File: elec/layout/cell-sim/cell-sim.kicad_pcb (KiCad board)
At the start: 2 copper layers, 225.7 x 100.8 mm, 0 parts

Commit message: single cell design + layout complete
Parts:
- added C1: 16V 100nF X7R ±10% 0402 Multilayer Ceramic Capacitors MLCC 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, lib:C0402, F.Cu at (20.3, 42.8)
- added C10: 25V 1uF X5R ±10% 0402 Multilayer Ceramic Capacitors MLCC - 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, lib:C0402, F.Cu at (110.1, 45.9)
- added C11: 50V 2.2uF X5R ±10% 0805 Multilayer Ceramic Capacitors MLCC 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, lib:C0805, F.Cu at (234.4, 151.8)
- added C12: 25V 10uF X5R ±10% 0805 Multilayer Ceramic Capacitors MLCC -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, lib:C0805, F.Cu at (234.4, 156.8)
- added C13: 25V 10uF X5R ±10% 0805 Multilayer Ceramic Capacitors MLCC -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, lib:C0805, F.Cu at (234.4, 111.8)
- added C14: 25V 10uF X5R ±10% 0805 Multilayer Ceramic Capacitors MLCC -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, lib:C0805, F.Cu at (234.4, 121.8)
- added C15: 16V 100nF X7R ±10% 0402 Multilayer Ceramic Capacitors MLCC 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, lib:C0402, F.Cu at (210.1, 158.6)
- added C16: 25V 10uF X5R ±10% 0805 Multilayer Ceramic Capacitors MLCC -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, lib:C0805, F.Cu at (240.8, 111.8)
- added C17: 25V 10uF X5R ±10% 0805 Multilayer Ceramic Capacitors MLCC -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, lib:C0805, F.Cu at (253.7, 111.8)
- added C18: 25V 10uF X5R ±10% 0805 Multilayer Ceramic Capacitors MLCC -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, lib:C0805, F.Cu at (260.2, 111.8)
- added C19: 16V 100nF X7R ±10% 0402 Multilayer Ceramic Capacitors MLCC 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, lib:C0402, F.Cu at (274.0, 82.9)
- added C2: 25V 10uF X5R ±10% 0805 Multilayer Ceramic Capacitors MLCC -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, lib:C0805, F.Cu at (18.8, 42.7)
- added C20: 25V 1uF X5R ±10% 0402 Multilayer Ceramic Capacitors MLCC - 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, lib:C0402, F.Cu at (267.5, 159.0)
- added C21: 25V 10uF X5R ±10% 0805 Multilayer Ceramic Capacitors MLCC -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, lib:C0805, F.Cu at (240.8, 126.8)
- added C22: 25V 10uF X5R ±10% 0805 Multilayer Ceramic Capacitors MLCC -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, lib:C0805, F.Cu at (240.8, 121.8)
- added C23: 16V 100nF X7R ±10% 0402 Multilayer Ceramic Capacitors MLCC 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, lib:C0402, F.Cu at (275.6, 122.5)
- added C24: 16V 100nF X7R ±10% 0402 Multilayer Ceramic Capacitors MLCC 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, lib:C0402, F.Cu at (282.2, 155.0)
- added C25: 25V 1uF X5R ±10% 0402 Multilayer Ceramic Capacitors MLCC - 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, lib:C0402, F.Cu at (283.7, 79.0)
- added C26: 25V 1uF X5R ±10% 0402 Multilayer Ceramic Capacitors MLCC - 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, lib:C0402, F.Cu at (282.2, 159.0)
- added C27: 50V 2.2uF X5R ±10% 0805 Multilayer Ceramic Capacitors MLCC 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, lib:C0805, F.Cu at (247.3, 111.8)
- added C28: 25V 10uF X5R ±10% 0805 Multilayer Ceramic Capacitors MLCC -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, lib:C0805, F.Cu at (266.6, 111.8)
- added C29: 25V 10uF X5R ±10% 0805 Multilayer Ceramic Capacitors MLCC -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, lib:C0805, F.Cu at (240.8, 116.8)
- added C3: 25V 10uF X5R ±10% 0805 Multilayer Ceramic Capacitors MLCC -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, lib:C0805, F.Cu at (16.7, 42.7)
- added C30: 25V 10uF X5R ±10% 0805 Multilayer Ceramic Capacitors MLCC -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, lib:C0805, F.Cu at (260.3, 105.0)
- added C31: 16V 100nF X7R ±10% 0402 Multilayer Ceramic Capacitors MLCC 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, lib:C0402, F.Cu at (278.9, 79.0)
- added C32: 25V 10uF X5R ±10% 0805 Multilayer Ceramic Capacitors MLCC -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, lib:C0805, F.Cu at (273.2, 105.0)
- added C33: 25V 10uF X5R ±10% 0805 Multilayer Ceramic Capacitors MLCC -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, lib:C0805, F.Cu at (234.4, 141.8)
- added C34: 25V 10uF X5R ±10% 0805 Multilayer Ceramic Capacitors MLCC -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, lib:C0805, F.Cu at (279.5, 111.8)
- added C35: 16V 100nF X7R ±10% 0402 Multilayer Ceramic Capacitors MLCC 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, lib:C0402, F.Cu at (277.4, 155.0)
- added C36: 25V 1uF X5R ±10% 0402 Multilayer Ceramic Capacitors MLCC - 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, lib:C0402, F.Cu at (280.4, 122.5)
- added C37: 25V 10uF X5R ±10% 0805 Multilayer Ceramic Capacitors MLCC -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, lib:C0805, F.Cu at (247.4, 105.0)
- added C38: 25V 10uF X5R ±10% 0805 Multilayer Ceramic Capacitors MLCC -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, lib:C0805, F.Cu at (273.1, 111.8)
- added C39: 16V 100nF X7R ±10% 0402 Multilayer Ceramic Capacitors MLCC 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, lib:C0402, F.Cu at (277.4, 159.0)
- added C4: 16V 100nF X7R ±10% 0402 Multilayer Ceramic Capacitors MLCC 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, lib:C0402, F.Cu at (67.9, 45.4)
- added C40: 16V 100nF X7R ±10% 0402 Multilayer Ceramic Capacitors MLCC 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, lib:C0402, F.Cu at (270.7, 122.5)
- added C41: 25V 1uF X5R ±10% 0402 Multilayer Ceramic Capacitors MLCC - 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, lib:C0402, F.Cu at (227.1, 157.2)
- added C42: 25V 1uF X5R ±10% 0402 Multilayer Ceramic Capacitors MLCC - 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, lib:C0402, F.Cu at (262.6, 159.0)
- added C43: 50V 2.2uF X5R ±10% 0805 Multilayer Ceramic Capacitors MLCC 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, lib:C0805, F.Cu at (234.4, 131.8)
- added C44: 25V 10uF X5R ±10% 0805 Multilayer Ceramic Capacitors MLCC -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, lib:C0805, F.Cu at (234.4, 146.8)
- added C45: 25V 10uF X5R ±10% 0805 Multilayer Ceramic Capacitors MLCC -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, lib:C0805, F.Cu at (240.8, 131.8)
- added C46: 25V 10uF X5R ±10% 0805 Multilayer Ceramic Capacitors MLCC -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, lib:C0805, F.Cu at (266.7, 105.0)
- added C47: 16V 100nF X7R ±10% 0402 Multilayer Ceramic Capacitors MLCC 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, lib:C0402, F.Cu at (205.3, 158.6)
- added C48: 25V 10uF X5R ±10% 0805 Multilayer Ceramic Capacitors MLCC -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, lib:C0805, F.Cu at (234.4, 126.8)
- added C49: 25V 10uF X5R ±10% 0805 Multilayer Ceramic Capacitors MLCC -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, lib:C0805, F.Cu at (279.6, 105.0)
- added C5: 16V 2.2uF X5R ±10% 0603 Multilayer Ceramic Capacitors MLCC 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, lib:C0603, F.Cu at (69.2, 45.3)
- added C50: 25V 10uF X5R ±10% 0805 Multilayer Ceramic Capacitors MLCC -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, lib:C0805, F.Cu at (234.4, 116.8)
- added C51: 16V 100nF X7R ±10% 0402 Multilayer Ceramic Capacitors MLCC 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, lib:C0402, F.Cu at (283.9, 116.2)
- added C52: 25V 1uF X5R ±10% 0402 Multilayer Ceramic Capacitors MLCC - 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, lib:C0402, F.Cu at (282.6, 89.3)
- added C53: 25V 10uF X5R ±10% 0805 Multilayer Ceramic Capacitors MLCC -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, lib:C0805, F.Cu at (253.8, 105.0)
- added C54: 25V 10uF X5R ±10% 0805 Multilayer Ceramic Capacitors MLCC -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, lib:C0805, F.Cu at (234.4, 136.8)
- added C55: 16V 100nF X7R ±10% 0402 Multilayer Ceramic Capacitors MLCC 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, lib:C0402, F.Cu at (274.0, 79.0)
- added C56: 16V 100nF X7R ±10% 0402 Multilayer Ceramic Capacitors MLCC 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, lib:C0402, F.Cu at (282.6, 93.2)
- added C57: 25V 1uF X5R ±10% 0402 Multilayer Ceramic Capacitors MLCC - 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, lib:C0402, F.Cu at (257.7, 159.0)
- added C58: 25V 1uF X5R ±10% 0402 Multilayer Ceramic Capacitors MLCC - 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, lib:C0402, F.Cu at (272.4, 159.0)
- added C6: 6.3V 10uF X5R ±20% 0402 Multilayer Ceramic Capacitors MLCC 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, lib:C0402, F.Cu at (94.7, 41.6)
- added C7: 25V 10uF X5R ±10% 0805 Multilayer Ceramic Capacitors MLCC -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, lib:C0805, F.Cu at (91.0, 41.7)
- added C8: 16V 100nF X7R ±10% 0402 Multilayer Ceramic Capacitors MLCC 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, lib:C0402, F.Cu at (94.5, 46.3)
- added C9: 25V 1uF X5R ±10% 0402 Multilayer Ceramic Capacitors MLCC - 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, lib:C0402, F.Cu at (114.6, 45.9)
- added DS1: , lib:SOD-323_L1.8-W1.3-LS2.5-RD, F.Cu at (94.9, 47.6)
- added DS2: , lib:SOD-323_L1.8-W1.3-LS2.5-RD, F.Cu at (240.8, 151.5)
- added L1: , lib:IND-SMD_L4.0-W4.0, F.Cu at (90.6, 45.4)
- added L2: , lib:IND-SMD_L4.4-W4.2, F.Cu at (220.3, 124.4)
- added L3: 100uH, lib:IND-SMD_L4.0-W4.0, F.Cu at (220.0, 139.3)
- added L4: , lib:IND-SMD_L4.4-W4.2, F.Cu at (220.3, 131.9)
- added L5: 100uH, lib:IND-SMD_L4.0-W4.0, F.Cu at (220.0, 146.7)
- added L6: , lib:IND-SMD_L4.4-W4.2, F.Cu at (220.3, 116.9)
- added L7: 100uH, lib:IND-SMD_L4.0-W4.0, F.Cu at (220.0, 154.0)
- added LED1: , lib:LED0603-RD, F.Cu at (247.1, 138.1)
- added LED2: , lib:LED0603-RD, F.Cu at (259.3, 122.8)
- added LED3: , lib:LED0603-RD, F.Cu at (265.3, 122.8)
- added LED4: , lib:LED0603-RD, F.Cu at (247.1, 156.7)
- added LED5: , lib:LED0603-RD, F.Cu at (247.1, 152.0)
- added LED6: , lib:LED0603-RD, F.Cu at (247.1, 142.7)
- added LED7: , lib:LED0603-RD, F.Cu at (247.1, 147.4)
- added LED8: , lib:LED0603-RD, F.Cu at (247.1, 133.4)
- added LED9: , lib:LED0603-RD, F.Cu at (253.2, 122.8)
- added Q1: , lib:SOT-23-3_L2.9-W1.3-P1.90-LS2.4-BR, F.Cu at (240.7, 156.9)
- added Q2: , lib:SOT-23-3_L2.9-W1.3-P1.90-LS2.4-BR, F.Cu at (259.7, 117.4)
- added Q3: , lib:SOT-23-3_L2.9-W1.3-P1.90-LS2.4-BR, F.Cu at (253.4, 117.4)
- added Q4: , lib:SOT-23-3_L2.9-W1.3-P1.90-LS2.4-BR, F.Cu at (272.2, 117.4)
- added Q5: , lib:SOT-23-3_L2.9-W1.3-P1.90-LS2.4-BR, F.Cu at (265.9, 117.4)
- added Q6: , lib:SOT-23-3_L2.9-W1.3-P1.90-LS2.4-BR, F.Cu at (247.2, 117.4)
- added R1: 62.5mW Thick Film Resistors 50V ±100ppm/℃ ±1% 10kΩ 0402 Chi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, lib:R0402, F.Cu at (19.7, 45.5)
- added R10: 62.5mW Thick Film Resistors 50V ±100ppm/℃ ±1% 10kΩ 0402 Chi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, lib:R0402, F.Cu at (78.4, 51.3)
- added R11: 62.5mW Thick Film Resistors 50V ±100ppm/℃ ±1% 10kΩ 0402 Chi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, lib:R0402, F.Cu at (77.3, 51.3)
- added R12: 62.5mW Thick Film Resistors 50V ±100ppm/℃ ±1% 10kΩ 0402 Chi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, lib:R0402, F.Cu at (77.2, 38.9)
- added R13: 62.5mW Thick Film Resistors 50V ±100ppm/℃ ±1% 10kΩ 0402 Chi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, lib:R0402, F.Cu at (78.2, 38.9)
- added R14: 62.5mW Thick Film Resistors 50V ±100ppm/℃ ±1% 10kΩ 0402 Chi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, lib:R0402, F.Cu at (75.1, 38.9)
- added R15: 62.5mW Thick Film Resistors 50V ±100ppm/℃ ±1% 10kΩ 0402 Chi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, lib:R0402, F.Cu at (76.1, 38.9)
- added R16: 62.5mW Thick Film Resistors 50V ±100ppm/℃ ±1% 10kΩ 0402 Chi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, lib:R0402, F.Cu at (73.0, 38.9)
- added R17: 62.5mW Thick Film Resistors 50V ±100ppm/℃ ±1% 10kΩ 0402 Chi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, lib:R0402, F.Cu at (74.0, 38.9)
- added R18: 62.5mW Thick Film Resistors 50V ±100ppm/℃ ±1% 10kΩ 0402 Chi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, lib:R0402, F.Cu at (70.9, 38.9)
- added R19: 62.5mW Thick Film Resistors 50V ±100ppm/℃ ±1% 10kΩ 0402 Chi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, lib:R0402, F.Cu at (71.9, 38.9)
- added R2: 62.5mW Thick Film Resistors 50V ±100ppm/℃ ±1% 4.7kΩ 0402 Ch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, lib:R0402, F.Cu at (50.3, 47.0)
- added R20: 62.5mW Thin Film Resistor 50V ±25ppm/℃ ±0.1% 22.6kΩ 0402 Ch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, lib:R0402, F.Cu at (92.1, 40.1)
- added R21: 62.5mW Thick Film Resistors 50V ±1% ±100ppm/℃ 4.12kΩ 0402 C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, lib:R0402, F.Cu at (90.2, 40.1)
- added R22: 62.5mW Thick Film Resistors 50V ±100ppm/℃ ±1% 17.4kΩ 0402 C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, lib:R0402, F.Cu at (111.4, 43.6)
- added R23: 62.5mW Thick Film Resistors 50V ±100ppm/℃ ±1% 10.2kΩ 0402 C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, lib:R0402, F.Cu at (113.4, 43.6)
- added R24: 62.5mW Thick Film Resistors 50V ±100ppm/℃ ±1% 10kΩ 0402 Chi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, lib:R0402, F.Cu at (130.3, 45.2)
- added R25: 62.5mW Thick Film Resistors 50V ±100ppm/℃ ±1% 10kΩ 0402 Chi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, lib:R0402, F.Cu at (127.7, 47.5)
- added R26: 62.5mW Thick Film Resistors 50V ±100ppm/℃ ±1% 21kΩ 0402 Chi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, lib:R0402, F.Cu at (267.6, 155.0)
- added R27: 62.5mW Thick Film Resistors 50V ±100ppm/℃ ±1% 24kΩ 0402 Chi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, lib:R0402, F.Cu at (257.7, 155.0)
- added R28: 62.5mW Thick Film Resistors 50V ±100ppm/℃ ±1% 37.4kΩ 0402 C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, lib:R0402, F.Cu at (272.5, 151.1)
- added R29: 62.5mW Thick Film Resistors 50V ±100ppm/℃ ±1% 10kΩ 0402 Chi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, lib:R0402, F.Cu at (267.6, 131.1)
- added R3: 62.5mW Thick Film Resistors 50V ±100ppm/℃ ±1% 4.7kΩ 0402 Ch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, lib:R0402, F.Cu at (53.3, 46.9)
- added R30: 62.5mW Thick Film Resistors 50V ±100ppm/℃ ±1% 10kΩ 0402 Chi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, lib:R0402, F.Cu at (277.4, 147.1)
- added R31: 62.5mW Thick Film Resistors 50V ±100ppm/℃ ±1% 43kΩ 0402 Chi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, lib:R0402, F.Cu at (267.6, 143.1)
- added R32: 62.5mW Thick Film Resistors 50V ±100ppm/℃ ±1% 60.4kΩ 0402 C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, lib:R0402, F.Cu at (267.6, 139.1)
- added R33: 62.5mW Thick Film Resistors 50V ±100ppm/℃ ±1% 10kΩ 0402 Chi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, lib:R0402, F.Cu at (262.6, 155.0)
- added R34: 62.5mW Thick Film Resistors 50V ±100ppm/℃ ±1% 10kΩ 0402 Chi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, lib:R0402, F.Cu at (277.4, 135.1)
- added R35: 125mW Thick Film Resistors 150V ±1% 100mΩ 0805 Chip Resisto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, lib:R0805, F.Cu at (240.8, 146.7)
- added R36: 62.5mW Thick Film Resistors 50V ±100ppm/℃ ±1% 21kΩ 0402 Chi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, lib:R0402, F.Cu at (257.7, 127.1)
- added R37: 62.5mW Thick Film Resistors 50V ±100ppm/℃ ±1% 10kΩ 0402 Chi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, lib:R0402, F.Cu at (267.6, 135.1)
- added R38: 62.5mW Thick Film Resistors 50V ±100ppm/℃ ±1% 1kΩ 0402 Chip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, lib:R0402, F.Cu at (277.4, 131.1)
- added R39: 62.5mW Thick Film Resistors 50V ±100ppm/℃ ±1% 21kΩ 0402 Chi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, lib:R0402, F.Cu at (267.6, 147.1)
- added R4: 62.5mW Thick Film Resistors 50V ±100ppm/℃ ±1% 10kΩ 0402 Chi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, lib:R0402, F.Cu at (71.9, 51.3)
- added R40: 62.5mW Thick Film Resistors 50V ±100ppm/℃ ±1% 10kΩ 0402 Chi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, lib:R0402, F.Cu at (272.5, 147.1)
- added R41: 62.5mW Thick Film Resistors 50V ±100ppm/℃ ±1% 1kΩ 0402 Chip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, lib:R0402, F.Cu at (257.7, 143.1)
- added R42: 62.5mW Thin Film Resistor 50V ±25ppm/℃ ±1% 11.5kΩ 0402 Chip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, lib:R0402, F.Cu at (272.5, 131.1)
- added R43: 62.5mW Thick Film Resistors 50V ±100ppm/℃ ±1% 6.2kΩ 0402 Ch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, lib:R0402, F.Cu at (267.6, 127.1)
- added R44: 62.5mW Thick Film Resistors 50V ±100ppm/℃ ±1% 21kΩ 0402 Chi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, lib:R0402, F.Cu at (272.5, 127.1)
- added R45: 62.5mW Thick Film Resistors 50V ±100ppm/℃ ±1% 24kΩ 0402 Chi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, lib:R0402, F.Cu at (282.3, 131.1)
- added R46: 62.5mW Thick Film Resistors 50V ±100ppm/℃ ±1% 37.4kΩ 0402 C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, lib:R0402, F.Cu at (282.3, 135.1)
- added R47: 62.5mW Thick Film Resistors 50V ±100ppm/℃ ±1% 10kΩ 0402 Chi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, lib:R0402, F.Cu at (262.6, 131.1)
- added R48: 62.5mW Thick Film Resistors 50V ±100ppm/℃ ±1% 10kΩ 0402 Chi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, lib:R0402, F.Cu at (267.6, 151.1)
- added R49: 62.5mW Thick Film Resistors 50V ±100ppm/℃ ±1% 43kΩ 0402 Chi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, lib:R0402, F.Cu at (282.3, 147.1)
- added R5: 62.5mW Thick Film Resistors 50V ±100ppm/℃ ±1% 10kΩ 0402 Chi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, lib:R0402, F.Cu at (70.9, 51.3)
- added R50: 62.5mW Thick Film Resistors 50V ±100ppm/℃ ±1% 60.4kΩ 0402 C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, lib:R0402, F.Cu at (252.6, 157.7)
- added R51: 62.5mW Thick Film Resistors 50V ±100ppm/℃ ±1% 10kΩ 0402 Chi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, lib:R0402, F.Cu at (282.3, 139.1)
- added R52: 62.5mW Thick Film Resistors 50V ±100ppm/℃ ±1% 10kΩ 0402 Chi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, lib:R0402, F.Cu at (262.6, 143.1)
- added R53: 125mW Thick Film Resistors 150V ±1% 100mΩ 0805 Chip Resisto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, lib:R0805, F.Cu at (240.8, 141.7)
- added R54: 62.5mW Thick Film Resistors 50V ±100ppm/℃ ±1% 21kΩ 0402 Chi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, lib:R0402, F.Cu at (257.7, 131.1)
- added R55: 62.5mW Thick Film Resistors 50V ±100ppm/℃ ±1% 10kΩ 0402 Chi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, lib:R0402, F.Cu at (262.6, 127.1)
- added R56: 62.5mW Thick Film Resistors 50V ±100ppm/℃ ±1% 1kΩ 0402 Chip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, lib:R0402, F.Cu at (277.4, 139.1)
- added R57: 62.5mW Thick Film Resistors 50V ±100ppm/℃ ±1% 21kΩ 0402 Chi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, lib:R0402, F.Cu at (252.6, 141.8)
- added R58: 62.5mW Thick Film Resistors 50V ±100ppm/℃ ±1% 10kΩ 0402 Chi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, lib:R0402, F.Cu at (262.6, 151.1)
- added R59: 62.5mW Thick Film Resistors 50V ±100ppm/℃ ±1% 1kΩ 0402 Chip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, lib:R0402, F.Cu at (257.7, 135.1)
- added R6: 62.5mW Thick Film Resistors 50V ±100ppm/℃ ±1% 10kΩ 0402 Chi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, lib:R0402, F.Cu at (74.1, 51.3)
- added R60: 62.5mW Thin Film Resistor 50V ±25ppm/℃ ±1% 11.5kΩ 0402 Chip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, lib:R0402, F.Cu at (252.6, 145.7)
- added R61: 62.5mW Thick Film Resistors 50V ±100ppm/℃ ±1% 6.2kΩ 0402 Ch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, lib:R0402, F.Cu at (257.7, 151.1)
- added R62: 62.5mW Thick Film Resistors 50V ±100ppm/℃ ±1% 21kΩ 0402 Chi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, lib:R0402, F.Cu at (252.6, 153.7)
- added R63: 62.5mW Thick Film Resistors 50V ±100ppm/℃ ±1% 24kΩ 0402 Chi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, lib:R0402, F.Cu at (262.6, 139.1)
- added R64: 62.5mW Thick Film Resistors 50V ±100ppm/℃ ±1% 37.4kΩ 0402 C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, lib:R0402, F.Cu at (282.3, 143.1)
- added R65: 62.5mW Thick Film Resistors 50V ±100ppm/℃ ±1% 10kΩ 0402 Chi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, lib:R0402, F.Cu at (272.5, 135.1)
- added R66: 62.5mW Thick Film Resistors 50V ±100ppm/℃ ±1% 10kΩ 0402 Chi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, lib:R0402, F.Cu at (272.5, 139.1)
- added R67: 62.5mW Thick Film Resistors 50V ±100ppm/℃ ±1% 43kΩ 0402 Chi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, lib:R0402, F.Cu at (257.7, 147.1)
- added R68: 62.5mW Thick Film Resistors 50V ±100ppm/℃ ±1% 60.4kΩ 0402 C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, lib:R0402, F.Cu at (262.6, 147.1)
- added R69: 62.5mW Thick Film Resistors 50V ±100ppm/℃ ±1% 10kΩ 0402 Chi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, lib:R0402, F.Cu at (252.6, 149.7)
- added R7: 62.5mW Thick Film Resistors 50V ±100ppm/℃ ±1% 10kΩ 0402 Chi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, lib:R0402, F.Cu at (73.0, 51.3)
- added R70: 62.5mW Thick Film Resistors 50V ±100ppm/℃ ±1% 10kΩ 0402 Chi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, lib:R0402, F.Cu at (262.6, 135.1)
- added R71: 125mW Thick Film Resistors 150V ±1% 100mΩ 0805 Chip Resisto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, lib:R0805, F.Cu at (240.8, 136.8)
- added R72: 62.5mW Thick Film Resistors 50V ±100ppm/℃ ±1% 21kΩ 0402 Chi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, lib:R0402, F.Cu at (282.3, 151.1)
- added R73: 62.5mW Thick Film Resistors 50V ±100ppm/℃ ±1% 10kΩ 0402 Chi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, lib:R0402, F.Cu at (272.5, 143.1)
- added R74: 62.5mW Thick Film Resistors 50V ±100ppm/℃ ±1% 1kΩ 0402 Chip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, lib:R0402, F.Cu at (277.4, 151.1)
- added R75: 62.5mW Thick Film Resistors 50V ±100ppm/℃ ±1% 21kΩ 0402 Chi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, lib:R0402, F.Cu at (277.4, 143.1)
- added R76: 62.5mW Thick Film Resistors 50V ±100ppm/℃ ±1% 10kΩ 0402 Chi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, lib:R0402, F.Cu at (272.5, 155.0)
- added R77: 62.5mW Thick Film Resistors 50V ±100ppm/℃ ±1% 1kΩ 0402 Chip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, lib:R0402, F.Cu at (257.7, 139.1)
- added R78: 62.5mW Thin Film Resistor 50V ±25ppm/℃ ±1% 11.5kΩ 0402 Chip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, lib:R0402, F.Cu at (277.4, 127.1)
- added R79: 62.5mW Thick Film Resistors 50V ±100ppm/℃ ±1% 6.2kΩ 0402 Ch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, lib:R0402, F.Cu at (282.3, 127.1)
- added R8: 62.5mW Thick Film Resistors 50V ±100ppm/℃ ±1% 10kΩ 0402 Chi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, lib:R0402, F.Cu at (76.2, 51.3)
- added R9: 62.5mW Thick Film Resistors 50V ±100ppm/℃ ±1% 10kΩ 0402 Chi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, lib:R0402, F.Cu at (75.2, 51.3)
- added U1: , lib:WIRELM-SMD_ESP32-S3-WROOM-1, F.Cu at (30.7, 51.1)
- added U10: , lib:SOT-23-6_L2.9-W1.6-P0.95-LS2.8-BL, F.Cu at (247.8, 99.3)
- added U11: , lib:SOT-23-6_L2.9-W1.6-P0.95-LS2.8-BL, F.Cu at (234.7, 99.3)
- added U12: , lib:SOT-23-6_L2.9-W1.6-P0.95-LS2.8-BL, F.Cu at (228.1, 99.3)
- added U13: , lib:WSON-6_L2.0-W2.0-P0.65-TL-EP, F.Cu at (247.3, 128.4)
- added U14: , lib:SOT-563_L1.6-W1.2-P0.50-LS1.6-TL, F.Cu at (252.7, 132.5)
- added U15: , lib:RELAY-SMD_HFD4-5-SR, F.Cu at (209.5, 104.6)
- added U16: , lib:RELAY-SMD_HFD4-5-SR, F.Cu at (209.5, 116.1)
- added U17: , lib:QFN-16_L3.0-W3.0-P0.50-BL-EP1.7, F.Cu at (240.9, 105.7)
- added U18: , lib:SOIC-8_L4.9-W3.9-P1.27-LS6.0-TL, F.Cu at (231.1, 92.0)
- added U19: , lib:LED-SMD_4P-L2.0-W2.0-BR, F.Cu at (250.4, 91.5)
- added U2: , lib:KEY-SMD_4P-L4.2-W3.2-P2.20-LS4.6, F.Cu at (17.5, 47.5)
- added U20: , lib:LED-SMD_4P-L2.0-W2.0-BR, F.Cu at (258.9, 91.5)
- added U21: , lib:SOT-23-5_L3.0-W1.7-P0.95-LS2.8-BL, F.Cu at (228.1, 118.6)
- added U22: , lib:PWRM-TH_BXXXXS-2WR2, F.Cu at (235.9, 79.5)
- added U23: , lib:MSOP-10_L3.0-W3.0-P0.50-LS5.0-BL, F.Cu at (228.0, 144.0)
- added U24: , lib:SOT-23-6_L2.9-W1.6-P0.95-LS2.8-BL, F.Cu at (267.6, 99.3)
- added U25: , lib:SOT-23-6_L2.9-W1.6-P0.95-LS2.8-BL, F.Cu at (261.0, 99.3)
- added U26: , lib:SOT-23-6_L2.9-W1.6-P0.95-LS2.8-BL, F.Cu at (274.1, 99.3)
- added U27: , lib:WSON-6_L2.0-W2.0-P0.65-TL-EP, F.Cu at (278.6, 116.9)
- added U28: , lib:SOT-563_L1.6-W1.2-P0.50-LS1.6-TL, F.Cu at (252.7, 127.7)
- added U29: , lib:RELAY-SMD_HFD4-5-SR, F.Cu at (209.5, 139.3)
- added U3: , lib:USB-C-SMD_KH-TYPE-C-16P, F.Cu at (51.6, 51.5)
- added U30: , lib:RELAY-SMD_HFD4-5-SR, F.Cu at (209.5, 127.7)
- added U31: , lib:QFN-16_L3.0-W3.0-P0.50-BL-EP1.7, F.Cu at (227.9, 151.6)
- added U32: , lib:SOIC-8_L4.9-W3.9-P1.27-LS6.0-TL, F.Cu at (221.1, 92.0)
- added U33: , lib:LED-SMD_4P-L2.0-W2.0-BR, F.Cu at (267.4, 91.5)
- added U34: , lib:LED-SMD_4P-L2.0-W2.0-BR, F.Cu at (275.9, 91.5)
- added U35: , lib:SOT-23-5_L3.0-W1.7-P0.95-LS2.8-BL, F.Cu at (228.1, 112.2)
- added U36: , lib:PWRM-TH_BXXXXS-2WR2, F.Cu at (258.8, 79.5)
- added U37: , lib:MSOP-10_L3.0-W3.0-P0.50-LS5.0-BL, F.Cu at (228.0, 126.3)
- added U38: , lib:SOT-23-6_L2.9-W1.6-P0.95-LS2.8-BL, F.Cu at (241.2, 99.3)
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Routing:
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- added copper zone on F.Cu, net buck.ic-sw
- added copper zone on F.Cu, net vcc
- added copper zone on F.Cu, net vcc-2
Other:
- board outline removed
- copper layers 2 -> 4

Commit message: layout progress
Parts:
- moved C24 232.8 mm to (55.3, 103.2), turned to -90 degrees
- moved C39 230.6 mm to (55.3, 96.9), turned to -90 degrees
- moved C56 227.4 mm to (55.3, 85.1), turned to -90 degrees
- moved C23 220.9 mm to (55.3, 106.0), turned to -90 degrees
- moved C55 218.9 mm to (55.3, 87.9), turned to -90 degrees
- moved U34 218.8 mm to (57.1, 93.9), turned to 180 degrees
- moved C40 217.3 mm to (55.3, 94.1), turned to -90 degrees
- moved U33 210.4 mm to (57.1, 96.7), turned to 180 degrees
- moved U20 202.2 mm to (57.0, 103.0), turned to 180 degrees
- moved C26 200.4 mm to (88.6, 107.0), turned to -90 degrees
- moved C25 199.1 mm to (86.6, 107.0), turned to -90 degrees
- moved C58 196.7 mm to (88.6, 88.9), turned to -90 degrees
- moved R79 196.4 mm to (89.7, 88.9), turned to -90 degrees
- moved R64 194.0 mm to (97.0, 85.3), turned to 90 degrees
- moved U19 193.9 mm to (57.0, 105.8), turned to 180 degrees
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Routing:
- net cell2-gnd-1: track 0.00 -> 91.9 mm, vias 0 -> 26
- net cell1-gnd: track 0.00 -> 91.9 mm, vias 0 -> 26
- net cell3-gnd-1: track 0.00 -> 91.9 mm, vias 0 -> 26
- net cell2-vcc-1: track 0.00 -> 87.6 mm, vias 0 -> 3
- net cell3-vcc-1: track 0.00 -> 87.6 mm, vias 0 -> 3
- net cell1-vcc-1: track 0.00 -> 87.6 mm, vias 0 -> 3
- net gnd: track 23.1 -> 67.0 mm, vias 4 -> 19
- net cell3-scl: track 0.00 -> 43.3 mm, vias 0 -> 5
- net cell1-scl: track 0.00 -> 43.3 mm, vias 0 -> 5
- net cell2-scl: track 0.00 -> 43.3 mm, vias 0 -> 5
- net cell3-sda: track 0.00 -> 40.6 mm, vias 0 -> 4
- net cell2-sda: track 0.00 -> 40.6 mm, vias 0 -> 4
- net cell1-sda: track 0.00 -> 40.6 mm, vias 0 -> 4
- net io41: track 0.00 -> 38.4 mm, vias 0 -> 6
- net cell2.dmm_relay-input: track 0.00 -> 38.0 mm, vias 0 -> 2
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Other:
- board text added: "CellN"
- board text added: "I"
- board text added: "V"

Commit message: layout complete
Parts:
- added J1: , lib:CONN-TH_XT30PW-M, F.Cu at (64.1, 127.1)
- added R20: 62.5mW Thick Film Resistors 50V ±100ppm/℃ ±1% 2.2kΩ 0402 Ch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, lib:R0402, F.Cu at (75.2, 124.5)
- added R21: 62.5mW Thick Film Resistors 50V ±100ppm/℃ ±1% 2.2kΩ 0402 Ch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, lib:R0402, F.Cu at (75.7, 121.4)
- added R82: 62.5mW Thick Film Resistors 50V ±100ppm/℃ ±1% 1kΩ 0402 Chip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, lib:R0402, F.Cu at (70.1, 75.9)
- added R83: 62.5mW Thick Film Resistors 50V ±100ppm/℃ ±1% 1kΩ 0402 Chip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, lib:R0402, F.Cu at (72.6, 75.9)
- added R84: 62.5mW Thick Film Resistors 50V ±100ppm/℃ ±1% 1kΩ 0402 Chip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, lib:R0402, F.Cu at (75.2, 75.9)
- added R85: 62.5mW Thick Film Resistors 50V ±100ppm/℃ ±1% 1kΩ 0402 Chip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, lib:R0402, F.Cu at (77.7, 75.9)
- added R86: 62.5mW Thick Film Resistors 50V ±100ppm/℃ ±1% 1kΩ 0402 Chip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, lib:R0402, F.Cu at (92.8, 76.2)
- added R87: 62.5mW Thick Film Resistors 50V ±100ppm/℃ ±1% 1kΩ 0402 Chip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, lib:R0402, F.Cu at (95.3, 76.2)
- added R88: 62.5mW Thick Film Resistors 50V ±100ppm/℃ ±1% 1kΩ 0402 Chip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, lib:R0402, F.Cu at (97.9, 76.2)
- added R89: 62.5mW Thick Film Resistors 50V ±100ppm/℃ ±1% 1kΩ 0402 Chip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, lib:R0402, F.Cu at (100.4, 76.2)
- added R90: 62.5mW Thick Film Resistors 50V ±100ppm/℃ ±1% 1kΩ 0402 Chip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, lib:R0402, F.Cu at (115.5, 76.2)
- added R91: 62.5mW Thick Film Resistors 50V ±100ppm/℃ ±1% 1kΩ 0402 Chip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, lib:R0402, F.Cu at (118.1, 76.2)
- added R92: 62.5mW Thick Film Resistors 50V ±100ppm/℃ ±1% 1kΩ 0402 Chip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, lib:R0402, F.Cu at (120.6, 76.2)
- added R93: 62.5mW Thick Film Resistors 50V ±100ppm/℃ ±1% 1kΩ 0402 Chip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, lib:R0402, F.Cu at (123.2, 76.2)
- added U4: , lib:AUDIO-TH_24.243.1, F.Cu at (130.3, 122.4)
- added U5: , lib:CONN-TH_24.243.2, F.Cu at (141.2, 122.6)
- added U52: , lib:HDR-SMD_8P-P2.54-V-M-R2-C4-LS7.4, F.Cu at (73.9, 70.4)
- added U53: , lib:HDR-SMD_8P-P2.54-V-M-R2-C4-LS7.4, F.Cu at (96.6, 70.6)
- added U54: , lib:HDR-SMD_8P-P2.54-V-M-R2-C4-LS7.4, F.Cu at (119.4, 70.6)
- R22: renamed from R20; value 62.5mW Thin Film Resistor 50V ±25ppm/℃ ±0.1% 22.6kΩ 0402 Chip Resistor - Surface Mount ROHS -> 62.5mW Thick Film Resistors 50V ±1% ±200ppm/℃ 22.6kΩ 0402 Chip Resistor - Surface Mount ROHS
- R34: renamed from R32; value 62.5mW Thick Film Resistors 50V ±100ppm/℃ ±1% 60.4kΩ 0402 Chip Resistor - Surface Mount ROHS -> 62.5mW Thick Film Resistors 50V ±100ppm/℃ ±1% 59kΩ 0402 Chip Resistor - Surface Mount ROHS
- R37: renamed from R35; value 125mW Thick Film Resistors 150V ±1% 100mΩ 0805 Chip Resistor - Surface Mount ROHS -> 125mW Thick Film Resistors ±600ppm/℃ ±1% 110mΩ 0805 Chip Resistor - Surface Mount ROHS
- R44: renamed from R42; value 62.5mW Thin Film Resistor 50V ±25ppm/℃ ±1% 11.5kΩ 0402 Chip Resistor - Surface Mount ROHS -> 62.5mW Thick Film Resistors 50V ±100ppm/℃ ±1% 11.5kΩ 0402 Chip Resistor - Surface Mount ROHS
- R52: renamed from R50; value 62.5mW Thick Film Resistors 50V ±100ppm/℃ ±1% 60.4kΩ 0402 Chip Resistor - Surface Mount ROHS -> 62.5mW Thick Film Resistors 50V ±100ppm/℃ ±1% 59kΩ 0402 Chip Resistor - Surface Mount ROHS
- R55: renamed from R53; value 125mW Thick Film Resistors 150V ±1% 100mΩ 0805 Chip Resistor - Surface Mount ROHS -> 125mW Thick Film Resistors ±600ppm/℃ ±1% 110mΩ 0805 Chip Resistor - Surface Mount ROHS
- R62: renamed from R60; value 62.5mW Thin Film Resistor 50V ±25ppm/℃ ±1% 11.5kΩ 0402 Chip Resistor - Surface Mount ROHS -> 62.5mW Thick Film Resistors 50V ±100ppm/℃ ±1% 11.5kΩ 0402 Chip Resistor - Surface Mount ROHS
- R70: renamed from R68; value 62.5mW Thick Film Resistors 50V ±100ppm/℃ ±1% 60.4kΩ 0402 Chip Resistor - Surface Mount ROHS -> 62.5mW Thick Film Resistors 50V ±100ppm/℃ ±1% 59kΩ 0402 Chip Resistor - Surface Mount ROHS
- R73: renamed from R71; value 125mW Thick Film Resistors 150V ±1% 100mΩ 0805 Chip Resistor - Surface Mount ROHS -> 125mW Thick Film Resistors ±600ppm/℃ ±1% 110mΩ 0805 Chip Resistor - Surface Mount ROHS
- R80: renamed from R78; value 62.5mW Thin Film Resistor 50V ±25ppm/℃ ±1% 11.5kΩ 0402 Chip Resistor - Surface Mount ROHS -> 62.5mW Thick Film Resistors 50V ±100ppm/℃ ±1% 11.5kΩ 0402 Chip Resistor - Surface Mount ROHS
- moved C5 5.38 mm to (68.8, 118.7)
- moved R10 5.38 mm to (74.7, 109.5)
- moved R11 5.38 mm to (74.7, 110.6)
- moved R16 5.38 mm to (62.3, 114.9)
- moved R19 5.38 mm to (62.3, 115.9)
- moved R4 5.38 mm to (74.7, 115.9)
- moved C4 5.38 mm to (68.8, 120.0)
- moved R12 5.38 mm to (62.3, 110.7)
- moved R13 5.38 mm to (62.3, 109.7)
- moved R14 5.38 mm to (62.3, 112.8)
- moved R15 5.38 mm to (62.3, 111.8)
- moved R17 5.38 mm to (62.3, 113.8)
- moved R18 5.38 mm to (62.3, 117.0)
- moved R5 5.38 mm to (74.7, 117.0)
- moved R6 5.38 mm to (74.7, 113.8)
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- renumbered R21 to R23, R22 to R24, R23 to R25, R24 to R26, R25 to R27, R26 to R28, R27 to R29, R28 to R30, R29 to R31, R30 to R32, R31 to R33, R33 to R35, R34 to R36, R36 to R38, R37 to R39, R38 to R40, R39 to R41, R40 to R42, R41 to R43, R43 to R45, R44 to R46, R45 to R47, R46 to R48, R47 to R49, R48 to R50, R49 to R51, R51 to R53, R52 to R54, R54 to R56, R55 to R57, R56 to R58, R57 to R59, R58 to R60, R59 to R61, R61 to R63, R62 to R64, R63 to R65, R64 to R66, R65 to R67, R66 to R68, R67 to R69, R69 to R71, R70 to R72, R72 to R74, R73 to R75, R74 to R76, R75 to R77, R76 to R78, R77 to R79, R79 to R81, U8 to U10, U9 to U11, U10 to U12, U11 to U13, U12 to U14, U13 to U15, U14 to U16, U15 to U17, U16 to U18, U17 to U19, U18 to U20, U19 to U21, U20 to U22, U21 to U23, U22 to U24, U23 to U25, U24 to U26, U25 to U27, U26 to U28, U27 to U29, U28 to U30, U29 to U31, U30 to U32, U31 to U33, U32 to U34, U33 to U35, U34 to U36, U35 to U37, U36 to U38, U37 to U39, U38 to U40, U39 to U41, U40 to U42, U41 to U43, U42 to U44, U43 to U45, U44 to U46, U45 to U47, U46 to U48, U47 to U49, U48 to U50, U49 to U51, U4 to U6, U5 to U7, U6 to U8, U7 to U9
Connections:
- C12 pad 2: cell1-gnd -> gnd
- C13 pad 2: cell1-gnd -> gnd
- C14 pad 2: cell1-gnd -> gnd
- C15 pad 2: cell1-gnd -> gnd
- C16 pad 2: cell1-gnd -> gnd
- C17 pad 2: cell1-gnd -> gnd
- C18 pad 2: cell1-gnd -> gnd
- C20 pad 2: cell1-gnd -> gnd
- C21 pad 2: cell1-gnd -> gnd
- C22 pad 1: cell1-cell -> cell1-gnd
- C22 pad 2: cell1-gnd -> gnd
- C25 pad 2: cell1-gnd -> gnd
- C26 pad 2: cell1-gnd -> gnd
- C28 pad 2: cell2-gnd-1 -> cell1-gnd
- C29 pad 2: cell2-gnd-1 -> cell1-gnd
- C30 pad 2: cell2-gnd-1 -> cell1-gnd
- C31 pad 2: cell2-gnd-1 -> cell1-gnd
- C32 pad 2: cell2-gnd-1 -> cell1-gnd
- C33 pad 2: cell2-gnd-1 -> cell1-gnd
- C34 pad 2: cell2-gnd-1 -> cell1-gnd
- C36 pad 2: cell2-gnd-1 -> cell1-gnd
- C37 pad 2: cell2-gnd-1 -> cell1-gnd
- C38 pad 1: cell2-cell -> cell2-gnd-1
- C38 pad 2: cell2-gnd-1 -> cell1-gnd
- C41 pad 2: cell2-gnd-1 -> cell1-gnd
- C42 pad 2: cell2-gnd-1 -> cell1-gnd
- C44 pad 2: cell3-gnd-1 -> cell2-gnd-1
- C45 pad 2: cell3-gnd-1 -> cell2-gnd-1
- C46 pad 2: cell3-gnd-1 -> cell2-gnd-1
- C47 pad 2: cell3-gnd-1 -> cell2-gnd-1
- C48 pad 2: cell3-gnd-1 -> cell2-gnd-1
- C49 pad 2: cell3-gnd-1 -> cell2-gnd-1
- C50 pad 2: cell3-gnd-1 -> cell2-gnd-1
- C52 pad 2: cell3-gnd-1 -> cell2-gnd-1
- C53 pad 2: cell3-gnd-1 -> cell2-gnd-1
- C54 pad 2: cell3-gnd-1 -> cell2-gnd-1
- C57 pad 2: cell3-gnd-1 -> cell2-gnd-1
- C58 pad 2: cell3-gnd-1 -> cell2-gnd-1
- L3 pad 2: cell1-cell -> cell1-gnd
- L5 pad 2: cell2-cell -> cell2-gnd-1
- Q1 pad 2: cell1-gnd -> gnd
- Q2 pad 2: cell1-gnd -> gnd
- Q3 pad 2: cell2-gnd-1 -> cell1-gnd
- Q4 pad 2: cell2-gnd-1 -> cell1-gnd
- Q5 pad 2: cell3-gnd-1 -> cell2-gnd-1
- Q6 pad 2: cell3-gnd-1 -> cell2-gnd-1
- R28 pad 2: cell1-gnd -> gnd
- R31 pad 2: cell1-gnd -> gnd
- R35 pad 2: cell1-gnd -> gnd
- R37 pad 1: cell1-cell -> cell1-gnd
- R40 pad 2: cell1-gnd -> gnd
- R43 pad 2: cell1-gnd -> gnd
- R45 pad 2: cell1-gnd -> gnd
- R46 pad 2: cell2-gnd-1 -> cell1-gnd
- R49 pad 2: cell2-gnd-1 -> cell1-gnd
- R53 pad 2: cell2-gnd-1 -> cell1-gnd
- R55 pad 1: cell2-cell -> cell2-gnd-1
- R58 pad 2: cell2-gnd-1 -> cell1-gnd
- R61 pad 2: cell2-gnd-1 -> cell1-gnd
- R63 pad 2: cell2-gnd-1 -> cell1-gnd
- R64 pad 2: cell3-gnd-1 -> cell2-gnd-1
- R67 pad 2: cell3-gnd-1 -> cell2-gnd-1
- R71 pad 2: cell3-gnd-1 -> cell2-gnd-1
- R76 pad 2: cell3-gnd-1 -> cell2-gnd-1
- R79 pad 2: cell3-gnd-1 -> cell2-gnd-1
- R81 pad 2: cell3-gnd-1 -> cell2-gnd-1
- U10 pad 4: cell1-gnd -> gnd
- U11 pad 1: cell1-gnd -> gnd
- U11 pad 3: cell1-gnd -> gnd
- U12 pad 2: cell1-gnd -> gnd
- U12 pad 6: cell1-gnd -> gnd
- U13 pad 1: cell1-gnd -> gnd
- U14 pad 2: cell1-gnd -> gnd
- U14 pad 6: cell1-gnd -> gnd
- U15 pad 3: cell1-gnd -> gnd
- U15 pad 7: cell1-gnd -> gnd
- U16 pad 2: cell1-gnd -> gnd
- U16 pad 3: cell1-cell -> cell1-gnd
- U16 pad 5: cell1-gnd -> gnd
- U17 pad 4: cell1-gnd -> gnd
- U18 pad 4: cell1-gnd -> gnd
- U19 pad 16: cell1-gnd -> gnd
- U19 pad 17: cell1-gnd -> gnd
- U19 pad 2: cell1.buck-enable -> cell1.gpio-p0
- U19 pad 3: cell1.ldo-enable -> cell1.gpio-p1
- U19 pad 4: cell1.gpio-p2 -> cell1.buck-enable
- U19 pad 5: cell1.gpio-p3 -> cell1.ldo-enable
- U19 pad 6: cell1-gnd -> gnd
- U20 pad 5: cell1-gnd -> gnd
- U23 pad 2: cell1-gnd -> gnd
- U24 pad 4: cell2-gnd-1 -> cell1-gnd
- U25 pad 1: cell2-gnd-1 -> cell1-gnd
- U25 pad 3: cell2-gnd-1 -> cell1-gnd
- U26 pad 2: cell2-gnd-1 -> cell1-gnd
- U26 pad 6: cell2-gnd-1 -> cell1-gnd
- U27 pad 1: cell2-gnd-1 -> cell1-gnd
- U28 pad 2: cell2-gnd-1 -> cell1-gnd
- U28 pad 6: cell2-gnd-1 -> cell1-gnd
- U29 pad 3: cell2-gnd-1 -> cell1-gnd
- U29 pad 7: cell2-gnd-1 -> cell1-gnd
- U30 pad 2: cell2-gnd-1 -> cell1-gnd
- U30 pad 3: cell2-cell -> cell2-gnd-1
- U30 pad 5: cell2-gnd-1 -> cell1-gnd
- U31 pad 4: cell2-gnd-1 -> cell1-gnd
- U32 pad 4: cell2-gnd-1 -> cell1-gnd
- U33 pad 16: cell2-gnd-1 -> cell1-gnd
- U33 pad 17: cell2-gnd-1 -> cell1-gnd
- U33 pad 2: cell2.buck-enable -> cell2.gpio-p0
- U33 pad 3: cell2.ldo-enable -> cell2.gpio-p1
- U33 pad 4: cell2.gpio-p2 -> cell2.buck-enable
- U33 pad 5: cell2.gpio-p3 -> cell2.ldo-enable
- U33 pad 6: cell2-gnd-1 -> cell1-gnd
- U34 pad 5: cell2-gnd-1 -> cell1-gnd
- U37 pad 2: cell2-gnd-1 -> cell1-gnd
- U38 pad 4: cell3-gnd-1 -> cell2-gnd-1
- U39 pad 1: cell3-gnd-1 -> cell2-gnd-1
- U39 pad 3: cell3-gnd-1 -> cell2-gnd-1
- U40 pad 2: cell3-gnd-1 -> cell2-gnd-1
- U40 pad 6: cell3-gnd-1 -> cell2-gnd-1
- U41 pad 1: cell3-gnd-1 -> cell2-gnd-1
- U42 pad 2: cell3-gnd-1 -> cell2-gnd-1
- U42 pad 6: cell3-gnd-1 -> cell2-gnd-1
- U43 pad 3: cell3-gnd-1 -> cell2-gnd-1
- U43 pad 7: cell3-gnd-1 -> cell2-gnd-1
- U44 pad 2: cell3-gnd-1 -> cell2-gnd-1
- U44 pad 5: cell3-gnd-1 -> cell2-gnd-1
- U45 pad 4: cell3-gnd-1 -> cell2-gnd-1
- U46 pad 4: cell3-gnd-1 -> cell2-gnd-1
- U47 pad 16: cell3-gnd-1 -> cell2-gnd-1
- U47 pad 17: cell3-gnd-1 -> cell2-gnd-1
- U47 pad 2: cell3.buck-enable -> cell3.gpio-p0
- U47 pad 3: cell3.ldo-enable -> cell3.gpio-p1
- U47 pad 4: cell3.gpio-p2 -> cell3.buck-enable
- U47 pad 5: cell3.gpio-p3 -> cell3.ldo-enable
- U47 pad 6: cell3-gnd-1 -> cell2-gnd-1
- U48 pad 5: cell3-gnd-1 -> cell2-gnd-1
- U51 pad 2: cell3-gnd-1 -> cell2-gnd-1
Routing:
- net gnd: track 67.0 -> 261.7 mm, vias 19 -> 54
- net micro.ic-sda: track 0.00 -> 104.2 mm, vias 0 -> 4
- net vcc-2: track 23.5 -> 125.3 mm, vias 6 -> 11
- net micro.ic-scl: track 0.00 -> 99.8 mm, vias 0 -> 4
- net cell3-gnd-1: track 91.9 -> 0.00 mm, vias 26 -> 0
- net vcc-3: track 16.3 -> 93.7 mm, vias 0 -> 15
- net cell2-gnd-1: track 91.9 -> 162.8 mm, vias 26 -> 32
- net vcc: track 13.0 -> 81.4 mm, vias 0 -> 1
- net gnd-2: track 0.00 -> 52.0 mm
- net vcc-4: track 0.00 -> 44.9 mm
- net dm: track 0.00 -> 40.5 mm, vias 0 -> 2
- net mux.ic-sda-3: track 2.94 -> 43.2 mm, vias 0 -> 3
- net dp: track 0.00 -> 39.1 mm, vias 0 -> 2
- net io41: track 38.4 -> 0.00 mm, vias 6 -> 0
- net hv_signal: track 5.81 -> 43.4 mm, vias 0 -> 2
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- added copper zone on B.Cu, net cell1-gnd
- added copper zone on In2.Cu, net cell1-gnd
- added copper zone on In1.Cu, net cell1-vcc-2
- added copper zone on B.Cu, net cell2-gnd-1
- added copper zone on In2.Cu, net cell2-gnd-1
- added copper zone on In1.Cu, net cell2-vcc-2
- added copper zone on In1.Cu, net cell3-vcc-2
- added copper zone on B.Cu, net gnd
- added copper zone on F.Cu, net gnd
- added copper zone on In2.Cu, net gnd
- added copper zone on B.Cu, net vcc-3
- added copper zone on In1.Cu, net vcc-3
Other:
- board outline added: 100 x 70 mm
- board text added: "12V Input"
- board text added: "Cell1"
- board text added: "Cell2"
- board text added: "Cell3"
- board text added: "Cell3 Voltage Domain!!!"
- board text added: "CellSim"
- board text added: "DMM"
- board text added: "I Out DMM 5V"
- board text added: "SCL SDA BUCK LDO"
- board text removed: "CellN"

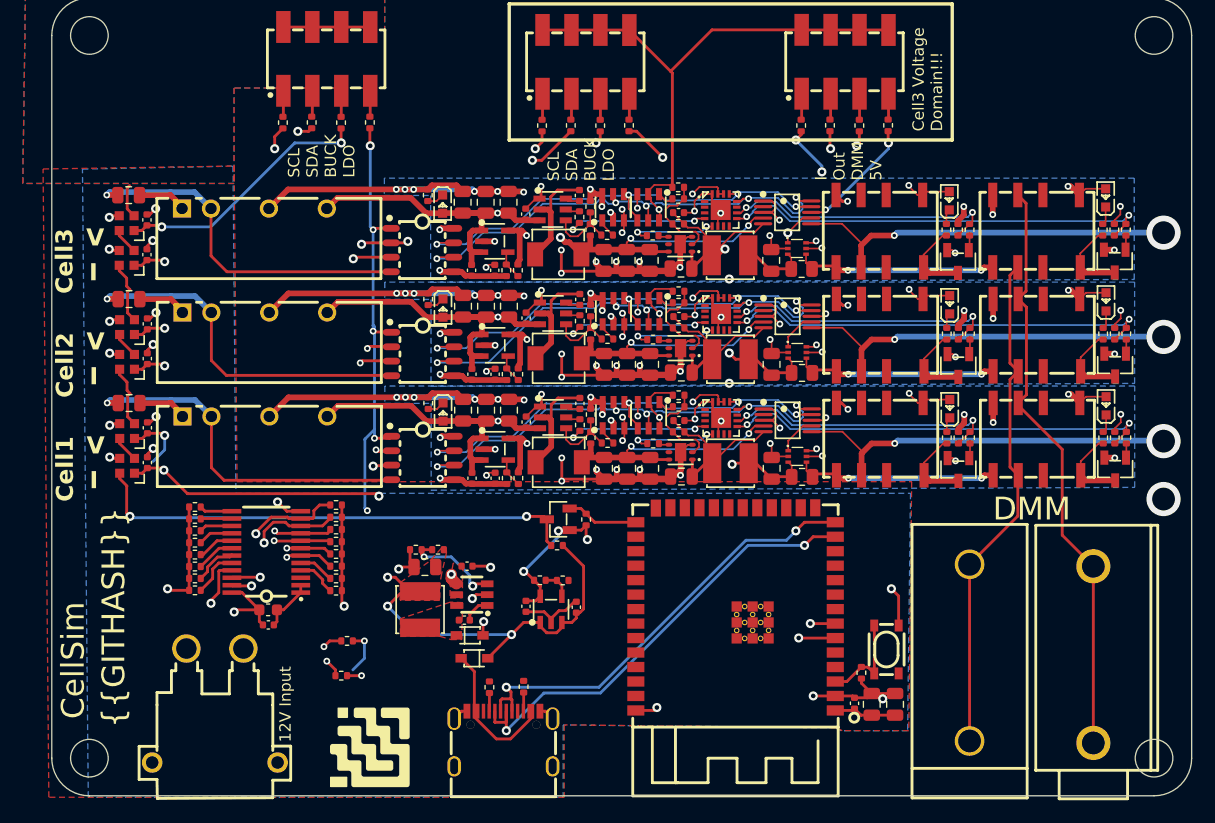
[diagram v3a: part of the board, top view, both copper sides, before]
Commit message: add reset pullup to i2c mux, add current limiting resistors to DMM connections, update layout
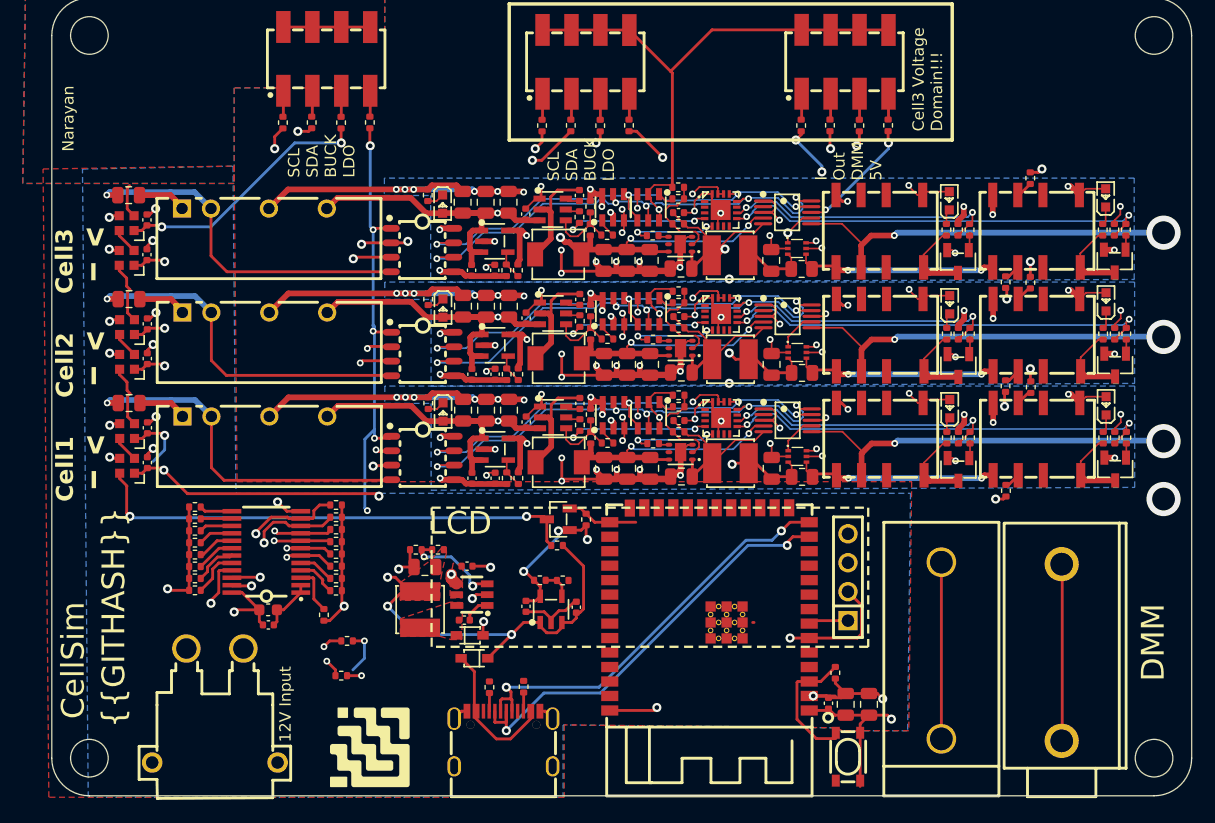
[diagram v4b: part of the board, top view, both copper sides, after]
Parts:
- added R4: 62.5mW Thick Film Resistors 50V ±100ppm/℃ ±1% 10kΩ 0402 Chi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, lib:R0402, F.Cu at (73.7, 119.1)
- added R47: 62.5mW Thick Film Resistors 50V ±100ppm/℃ ±1% 10kΩ 0402 Chi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, lib:R0402, F.Cu at (133.5, 108.2)
- added R48: 62.5mW Thick Film Resistors 50V ±100ppm/℃ ±1% 10kΩ 0402 Chi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, lib:R0402, F.Cu at (135.7, 99.1)
- added R67: 62.5mW Thick Film Resistors 50V ±100ppm/℃ ±1% 10kΩ 0402 Chi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, lib:R0402, F.Cu at (133.5, 99.1)
- added R68: 62.5mW Thick Film Resistors 50V ±100ppm/℃ ±1% 10kΩ 0402 Chi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, lib:R0402, F.Cu at (135.6, 90.0)
- added R87: 62.5mW Thick Film Resistors 50V ±100ppm/℃ ±1% 10kΩ 0402 Chi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, lib:R0402, F.Cu at (133.5, 89.9)
- added R88: 62.5mW Thick Film Resistors 50V ±100ppm/℃ ±1% 10kΩ 0402 Chi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, lib:R0402, F.Cu at (135.6, 80.8)
- added U6: , lib:HDR-TH_4P-P2.54-V-F, F.Cu at (119.6, 115.8)
- moved U2 10.00 mm to (119.6, 131.6)
- moved U5 2.78 mm to (138.4, 122.4)
- moved U4 2.48 mm to (127.8, 122.3)
- moved C1 2.29 mm to (117.9, 126.9)
- moved C2 2.29 mm to (119.4, 127.0)
- moved C3 2.29 mm to (121.5, 127.0)
- moved R1 2.29 mm to (118.5, 124.2)
- moved U1 2.29 mm to (107.5, 118.6)
- renumbered R9 to R10, R93 to R100, R10 to R11, R11 to R12, R12 to R13, R13 to R14, R14 to R15, R15 to R16, R16 to R17, R17 to R18, R18 to R19, R19 to R20, R20 to R21, R21 to R22, R22 to R23, R23 to R24, R24 to R25, R25 to R26, R26 to R27, R27 to R28, R28 to R29, R29 to R30, R30 to R31, R31 to R32, R32 to R33, R33 to R34, R34 to R35, R35 to R36, R36 to R37, R37 to R38, R38 to R39, R39 to R40, R40 to R41, R41 to R42, R42 to R43, R43 to R44, R44 to R45, R45 to R46, R46 to R49, R4 to R5, R47 to R50, R48 to R51, R49 to R52, R50 to R53, R51 to R54, R52 to R55, R53 to R56, R54 to R57, R55 to R58, R56 to R59, R5 to R6, R57 to R60, R58 to R61, R59 to R62, R60 to R63, R61 to R64, R62 to R65, R63 to R66, R64 to R69, R6 to R7, R65 to R70, R66 to R71, R67 to R72, R68 to R73, R69 to R74, R70 to R75, R71 to R76, R72 to R77, R73 to R78, R74 to R79, R7 to R8, R75 to R80, R76 to R81, R77 to R82, R78 to R83, R79 to R84, R80 to R85, R81 to R86, R82 to R89, R8 to R9, R83 to R90, R84 to R91, R85 to R92, R86 to R93, R87 to R94, R88 to R95, R89 to R96, R90 to R97, R91 to R98, R92 to R99, U9 to U10, U10 to U11, U11 to U12, U12 to U13, U13 to U14, U14 to U15, U15 to U16, U16 to U17, U17 to U18, U18 to U19, U19 to U20, U20 to U21, U21 to U22, U22 to U23, U23 to U24, U24 to U25, U25 to U26, U26 to U27, U27 to U28, U28 to U29, U29 to U30, U30 to U31, U31 to U32, U32 to U33, U33 to U34, U34 to U35, U35 to U36, U36 to U37, U37 to U38, U38 to U39, U39 to U40, U40 to U41, U41 to U42, U42 to U43, U43 to U44, U44 to U45, U45 to U46, U46 to U47, U47 to U48, U48 to U49, U49 to U50, U50 to U51, U51 to U52, U52 to U53, U53 to U54, U54 to U55, U6 to U7, U7 to U8, U8 to U9
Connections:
- U13 pad 6: gnd -> cell1-vcc-1
- U19 pad 3: gnd-2 -> cell1.dmm_relay-gnd
- U19 pad 6: vcc-4 -> cell1.dmm_relay-vcc
- U27 pad 6: cell1-gnd -> cell2-vcc-1
- U33 pad 3: gnd-2 -> cell2.dmm_relay-gnd
- U33 pad 6: vcc-4 -> cell2.dmm_relay-vcc
- U41 pad 6: cell2-gnd-1 -> cell3-vcc-1
- U47 pad 3: gnd-2 -> cell3.dmm_relay-gnd
- U47 pad 6: vcc-4 -> cell3.dmm_relay-vcc
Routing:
- net micro.ic-scl: track 99.8 -> 113.9 mm
- net gnd: track 261.7 -> 268.6 mm
- net gnd-2: track 52.0 -> 58.4 mm, vias 0 -> 3
- net reset_: track 0.00 -> 4.21 mm
- net micro.ic-sda: track 104.2 -> 108.1 mm, vias 4 -> 3
- net micro.ic-en: track 8.40 -> 11.3 mm
- net cell1.dmm_relay-vcc: track 0.00 -> 2.47 mm
- net vcc-3: track 93.7 -> 96.0 mm
- net dp: track 39.1 -> 36.8 mm
- net dm: track 40.5 -> 38.4 mm
- net cell1.dmm_relay-gnd: track 0.00 -> 1.68 mm
- net cell3.dmm_relay-gnd: track 0.00 -> 1.49 mm
- net cell2.dmm_relay-gnd: track 0.00 -> 1.45 mm
- net cell2.dmm_relay-vcc: track 0.00 -> 1.44 mm
- net cell3.dmm_relay-vcc: track 0.00 -> 1.39 mm
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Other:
- board text added: "LCD"
- board text added: "Narayan"
